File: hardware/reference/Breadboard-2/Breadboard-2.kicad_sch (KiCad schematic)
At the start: 71 parts, among them J1 01x06, J2 01x06, J3 01x05, J4 01x07, J5 01x05S, Q31 BSS138K, Q51 SSM3J356R,LF, Q52 SSM3J356R,LF, Q53 DTC143ZCA, Q54 DTC143ZCA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

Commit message: Correct data sheet link.
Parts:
- U21: Cost (none) -> 1.60; LCSC (none) -> C529334; MPN (none) -> STM32G031F8P6; Specification (none) -> 64KB 1.7V~3.6V ARM-MSeries 8KB 64MHz FLASH 18 TSSOP-20 Micr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
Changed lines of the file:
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@@
       (effects (font (size 1.27 1.27)) (justify right) hide)
     )
-    (property "Datasheet" "https://www.st.com/resource/en/datasheet/stm32g071kb.pdf" (id 3) (at 78.105 123.19 0)
+    (property "Datasheet" "https://www.st.com/resource/en/datasheet/stm32g031f8.pdf" (id 3) (at 78.105 123.19 0)
       (effects (font (size 1.27 1.27)) hide)
     )
+    (property "Cost" "1.60" (id 4) (at 47.625 96.52 0)
+      (effects (font (size 1.27 1.27)) hide)
+    )
+    (property "LCSC" "C529334" (id 5) (at 47.625 96.52 0)
+      (effects (font (size 1.27 1.27)) hide)
+    )
+    (property "MPN" "STM32G031F8P6" (id 6) (at 47.625 96.52 0)
+      (effects (font (size 1.27 1.27)) hide)
+    )
+    (property "Specification" "64KB 1.7V~3.6V ARM-MSeries 8KB 64MHz FLASH 18 TSSOP-20 Microcontroller Units" (id 7) (at 47.625 96.52 0)
+      (effects (font (size 1.27 1.27)) hide)
+    )

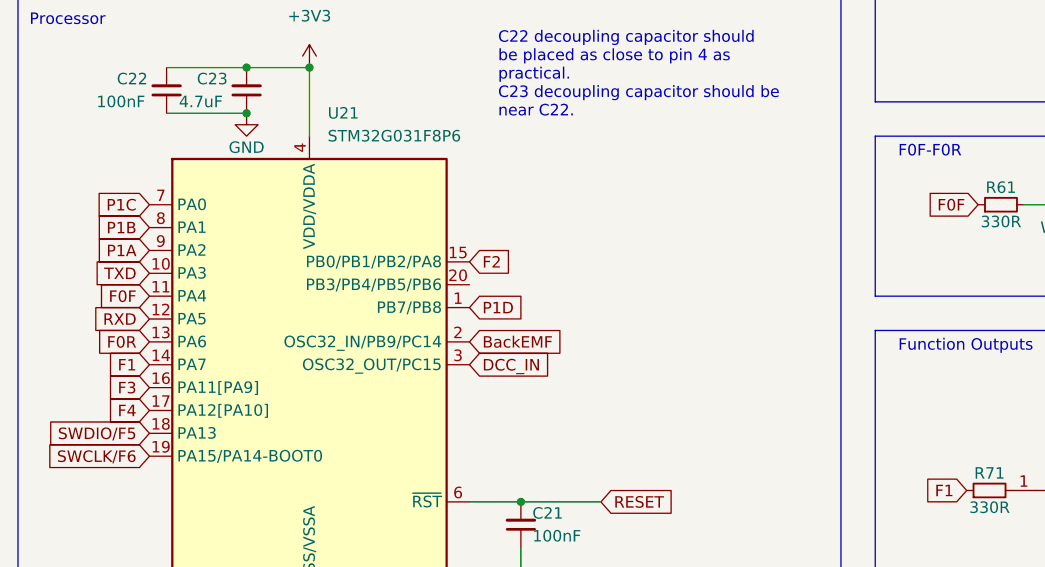
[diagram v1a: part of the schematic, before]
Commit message: Move DCC_IN and BackEMF to pins with appropriate capabilities.
STM32 does not allow software remapping of the periperhal input
pins.  The location in the PIC design (Breadboard-1) routes them
to pins on an STM32 that are designed for the oscellator, but can
be re-used.  As such they have no ADC or Timer triggers attached
to them.

DCC_IN was moved to port 20, which can be routed to any of
TIM1_CH2, TIM2_CH2, TIM3_CH1, TIM3_CH2, TIM1_CH3, TIM16_CH1N.

BackEMF was moved to pin 7, which can be routed to ADC_IN0.

The displaced P1C H-Bridge output was moved to pin 2, as it's more
than capable of outputting the necessary signal.
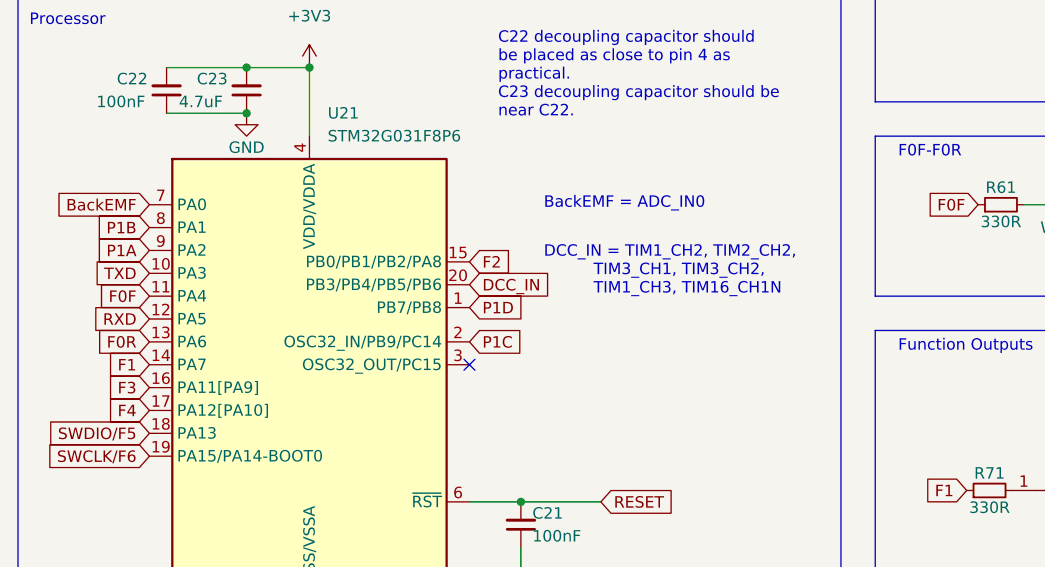
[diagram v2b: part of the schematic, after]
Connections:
- net BackEMF: now also U21.7 (PA0); no longer U21.2 (OSC32_IN/PB9/PC14)
- net DCC_IN: now also U21.20 (PB3/PB4/PB5/PB6); no longer U21.3 (OSC32_OUT/PC15)
- net P1C: now also U21.2 (OSC32_IN/PB9/PC14); no longer U21.7 (PA0)
- no-connect marks 2 -> 3
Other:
- note added: "BackEMF = ADC_IN0"
- note added: "DCC_IN = TIM1_CH2, TIM2_CH2, TIM3_CH1, TIM3_CH2, TIM1_CH3, TIM16_CH1N"
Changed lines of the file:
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@@
   (no_connect (at 254 83.82))
   (no_connect (at 254 73.66))
+  (no_connect (at 65.405 93.98))
   (wire (pts (xy 242.57 62.23) (xy 255.27 62.23))
     (stroke (width 0) (type default) (color 0 0 0 0))
@@
     (effects (font (size 1.27 1.27)) (justify left bottom))
   )
+  (text "BackEMF = ADC_IN0" (at 73.66 76.835 0)
+    (effects (font (size 1.27 1.27)) (justify left bottom))
+  )
   (text "Function Outputs" (at 113.03 92.71 0)
     (effects (font (size 1.27 1.27)) (justify left bottom))
@@
   )
   (text "Motor Drive" (at 111.76 17.78 0)
+    (effects (font (size 1.27 1.27)) (justify left bottom))
+  )
+  (text "DCC_IN = TIM1_CH2, TIM2_CH2,\n          TIM3_CH1, TIM3_CH2,\n          TIM1_CH3, TIM16_CH1N"
+    (at 73.66 86.36 0)
     (effects (font (size 1.27 1.27)) (justify left bottom))
   )
@@
     )
   )
-  (global_label "P1C" (shape input) (at 29.845 76.2 180) (fields_autoplaced)
-    (effects (font (size 1.27 1.27)) (justify right))
-    (property "Intersheet References" "${INTERSHEET_REFS}" (id 0) (at 23.6824 76.2794 0)
-      (effects (font (size 1.27 1.27)) (justify right) hide)
+  (global_label "P1C" (shape input) (at 65.405 91.44 0) (fields_autoplaced)
+    (effects (font (size 1.27 1.27)) (justify left))
+    (property "Intersheet References" "${INTERSHEET_REFS}" (id 0) (at 71.5676 91.3606 0)
+      (effects (font (size 1.27 1.27)) (justify left) hide)
     )
   )
@@
     )
   )
-  (global_label "DCC_IN" (shape input) (at 65.405 93.98 0) (fields_autoplaced)
-    (effects (font (size 1.27 1.27)) (justify left))
-    (property "Intersheet References" "${INTERSHEET_REFS}" (id 0) (at 74.531 93.9006 0)
+  (global_label "DCC_IN" (shape input) (at 65.405 85.09 0) (fields_autoplaced)
+    (effects (font (size 1.27 1.27)) (justify left))
+    (property "Intersheet References" "${INTERSHEET_REFS}" (id 0) (at 74.531 85.0106 0)
       (effects (font (size 1.27 1.27)) (justify left) hide)
     )
@@
     )
   )
-  (global_label "BackEMF" (shape input) (at 65.405 91.44 0) (fields_autoplaced)
-    (effects (font (size 1.27 1.27)) (justify left))
-    (property "Intersheet References" "${INTERSHEET_REFS}" (id 0) (at 76.0429 91.5194 0)
-      (effects (font (size 1.27 1.27)) (justify left) hide)
-    )
-  )
+  (global_label "BackEMF" (shape input) (at 29.845 76.2 180) (fields_autoplaced)
+    (effects (font (size 1.27 1.27)) (justify right))
+    (property "Intersheet References" "${INTERSHEET_REFS}" (id 0) (at 19.2071 76.1206 0)
+      (effects (font (size 1.27 1.27)) (justify right) hide)
+    )
+  )
